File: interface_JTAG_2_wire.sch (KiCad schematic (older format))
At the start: 5 parts

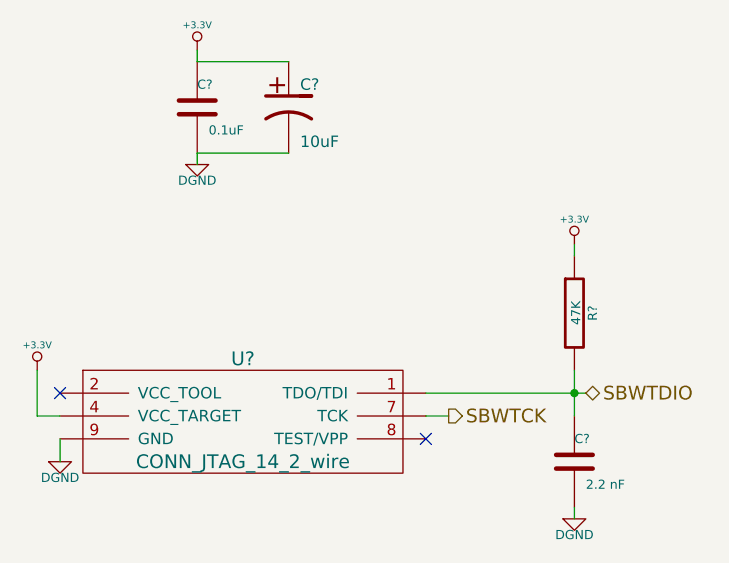
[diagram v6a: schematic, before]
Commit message: various fixes due to issues found in ERC
learned how to use invisible pins
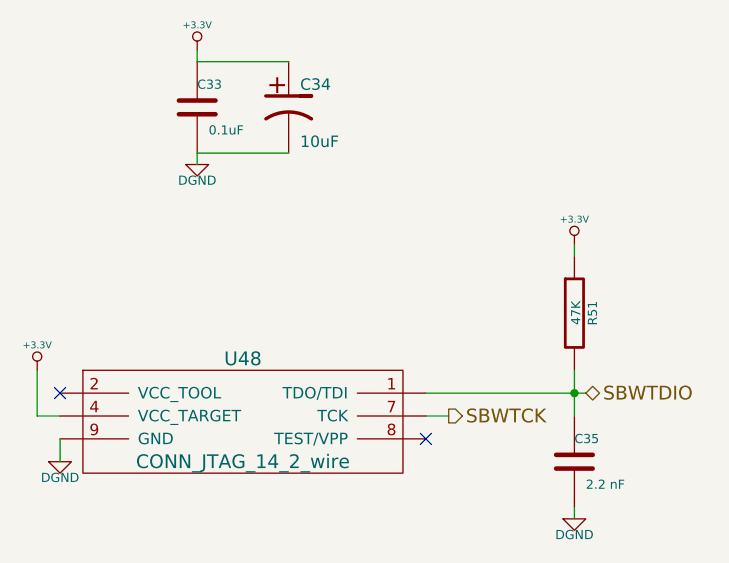
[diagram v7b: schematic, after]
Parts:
- gave numbers to parts that had none: 5
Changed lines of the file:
@@
 Sheet 16 18
 Title ""
-Date "18 dec 2013"
+Date "20 dec 2013"
 Rev ""
 Comp ""
@@
 $EndDescr
 $Comp
-L CONN_JTAG_14 U?
+L CONN_JTAG_14 U48
 U 1 1 52A68398
 P 4450 2100
-F 0 "U?" H 4450 2100 60  0000 C CNN
+F 0 "U48" H 4450 2100 60  0000 C CNN
 F 1 "CONN_JTAG_14_2_wire" H 4450 1650 60  0000 C CNN
 F 2 "" H 4450 2100 60  0000 C CNN
@@
 $EndComp
 $Comp
-L C C?
+L C C33
 U 1 1 52A6994D
 P 4250 1000
-F 0 "C?" H 4250 1100 40  0000 L CNN
+F 0 "C33" H 4250 1100 40  0000 L CNN
 F 1 "0.1uF" H 4300 900 40  0000 L CNN
 F 2 "~" H 4288 850 30  0000 C CNN
@@
 $EndComp
 $Comp
-L +3.3V #PWR?
+L +3.3V #PWR0109
 U 1 1 52A69953
 P 4250 750
-F 0 "#PWR?" H 4250 710 30  0001 C CNN
+F 0 "#PWR0109" H 4250 710 30  0001 C CNN
 F 1 "+3.3V" H 4250 860 30  0000 C CNN
 F 2 "" H 4250 750 60  0000 C CNN
@@
 $EndComp
 $Comp
-L DGND #PWR?
+L DGND #PWR0110
 U 1 1 52A69959
 P 4250 1250
-F 0 "#PWR?" H 4250 1250 40  0001 C CNN
+F 0 "#PWR0110" H 4250 1250 40  0001 C CNN
 F 1 "DGND" H 4250 1180 40  0000 C CNN
 F 2 "" H 4250 1250 60  0000 C CNN
@@
 	4250 1200 4250 1250
 $Comp
-L +3.3V #PWR?
+L +3.3V #PWR0111
 U 1 1 52A69961
 P 3550 2150
-F 0 "#PWR?" H 3550 2110 30  0001 C CNN
+F 0 "#PWR0111" H 3550 2110 30  0001 C CNN
 F 1 "+3.3V" H 3550 2260 30  0000 C CNN
 F 2 "" H 3550 2150 60  0000 C CNN
@@
 	3550 2350 3650 2350
 $Comp
-L DGND #PWR?
+L DGND #PWR0112
 U 1 1 52A69987
 P 3650 2550
-F 0 "#PWR?" H 3650 2550 40  0001 C CNN
+F 0 "#PWR0112" H 3650 2550 40  0001 C CNN
 F 1 "DGND" H 3650 2480 40  0000 C CNN
 F 2 "" H 3650 2550 60  0000 C CNN
@@
 SBWTCK
 $Comp
-L CP1 C?
+L CP1 C34
 U 1 1 52A699A3
 P 4650 1000
-F 0 "C?" H 4700 1100 50  0000 L CNN
+F 0 "C34" H 4700 1100 50  0000 L CNN
 F 1 "10uF" H 4700 850 50  0000 L CNN
 F 2 "~" H 4650 1000 60  0000 C CNN
@@
 SBWTDIO
 $Comp
-L R R?
+L R R51
 U 1 1 52A69CB1
 P 5900 1900
-F 0 "R?" V 5980 1900 40  0000 C CNN
+F 0 "R51" V 5980 1900 40  0000 C CNN
 F 1 "47K" V 5907 1901 40  0000 C CNN
 F 2 "~" V 5830 1900 30  0000 C CNN
@@
 $EndComp
 $Comp
-L C C?
+L C C35
 U 1 1 52A69CB7
 P 5900 2550
-F 0 "C?" H 5900 2650 40  0000 L CNN
+F 0 "C35" H 5900 2650 40  0000 L CNN
 F 1 "2.2 nF" H 5950 2450 40  0000 L CNN
 F 2 "~" H 5938 2400 30  0000 C CNN
@@
 Connection ~ 5900 2250
 $Comp
-L +3.3V #PWR?
+L +3.3V #PWR0113
 U 1 1 52A69CDC
 P 5900 1600
-F 0 "#PWR?" H 5900 1560 30  0001 C CNN
+F 0 "#PWR0113" H 5900 1560 30  0001 C CNN
 F 1 "+3.3V" H 5900 1710 30  0000 C CNN
 F 2 "" H 5900 1600 60  0000 C CNN
@@
 	5900 1600 5900 1650
 $Comp
-L DGND #PWR?
+L DGND #PWR0114
 U 1 1 52A69CF0
 P 5900 2800
-F 0 "#PWR?" H 5900 2800 40  0001 C CNN
+F 0 "#PWR0114" H 5900 2800 40  0001 C CNN
 F 1 "DGND" H 5900 2730 40  0000 C CNN
 F 2 "" H 5900 2800 60  0000 C CNN
